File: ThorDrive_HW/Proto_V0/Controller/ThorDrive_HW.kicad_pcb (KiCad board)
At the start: 2 copper layers, 98.5 x 99 mm, 46 parts, among them J1 Conn_01x04_Socket, J10 Conn_01x03_Socket, J2 Conn_01x06_Socket, J3 Conn_01x03_Socket, J4 Conn_01x08_Socket, J5 Conn_01x08_Pin, J6 Conn_01x04_Pin, J7 Conn_01x06_Pin, J8 Conn_01x04_Pin, J9 Conn_01x04_Pin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

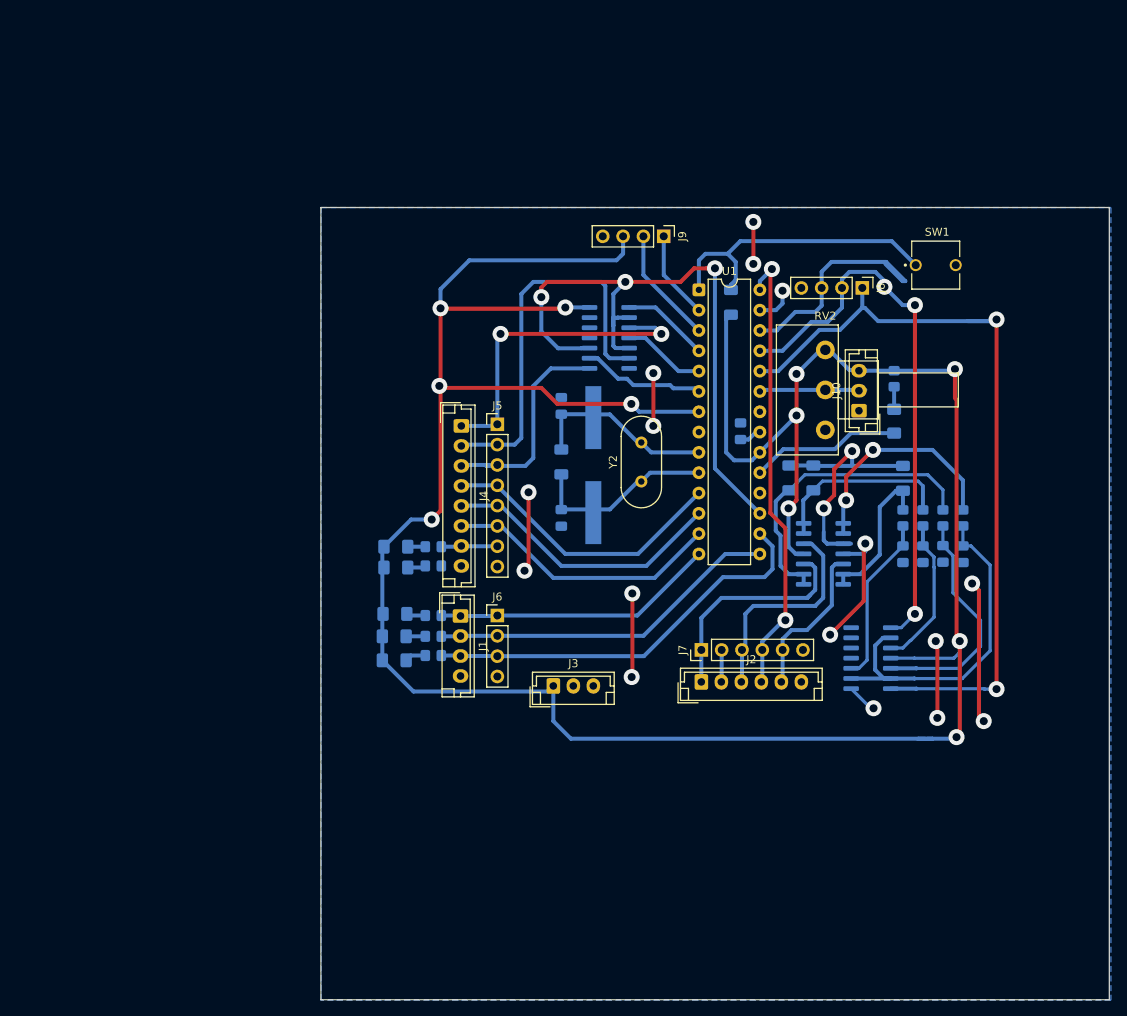
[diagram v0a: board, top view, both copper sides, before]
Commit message: Controller Board V0 Finalized
A Controller Board simple and built upon the Atmega328p...
Single Layer Design with few jumpers.... Compatible with Inverter V0
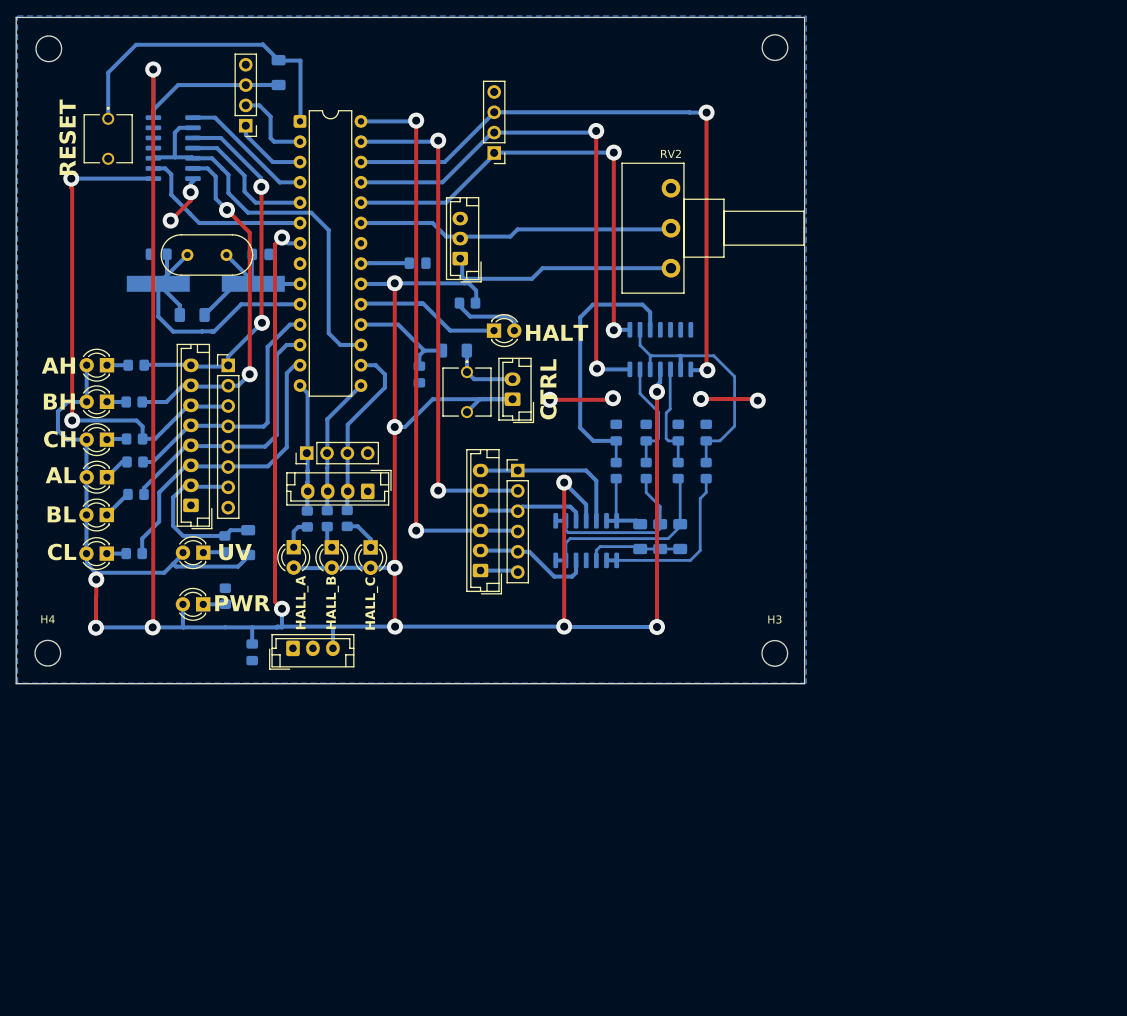
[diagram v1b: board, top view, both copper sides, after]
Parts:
- added C8: 10u, Capacitor_SMD:C_0805_2012Metric_Pad1.18x1.45mm_HandSolder, B.Cu at (53.4, 100.8)
- added C9: 100n, Capacitor_SMD:C_0805_2012Metric_Pad1.18x1.45mm_HandSolder, B.Cu at (74.3, 66.1)
- added D10: AL, LED_THT:LED_D3.0mm, F.Cu at (35.2, 78.9)
- added D11: BL, LED_THT:LED_D3.0mm, F.Cu at (35.2, 83.6)
- added D12: CL, LED_THT:LED_D3.0mm, F.Cu at (35.2, 88.5)
- added D7: AH, LED_THT:LED_D3.0mm, F.Cu at (35.2, 64.9)
- added D8: BH, LED_THT:LED_D3.0mm, F.Cu at (35.2, 69.5)
- added D9: CH, LED_THT:LED_D3.0mm, F.Cu at (35.2, 74.2)
- added H1: MountingHole, MountingHole:MountingHole_3.2mm_M3, F.Cu at (27.9, 25.4)
- added H2: MountingHole, MountingHole:MountingHole_3.2mm_M3, F.Cu at (118.7, 25.2)
- added H3: MountingHole, MountingHole:MountingHole_3.2mm_M3, F.Cu at (118.7, 100.9)
- added H4: MountingHole, MountingHole:MountingHole_3.2mm_M3, F.Cu at (27.8, 100.9)
- added J13: CTRL, Connector_JST:JST_EH_B2B-EH-A_1x02_P2.50mm_Vertical, F.Cu at (85.9, 69.2)
- added R16: 1k, Resistor_SMD:R_0805_2012Metric_Pad1.20x1.40mm_HandSolder, B.Cu at (38.9, 64.9)
- added R17: 1k, Resistor_SMD:R_0805_2012Metric_Pad1.20x1.40mm_HandSolder, B.Cu at (38.6, 69.5)
- added R18: 1k, Resistor_SMD:R_0805_2012Metric_Pad1.20x1.40mm_HandSolder, B.Cu at (38.7, 74.1)
- added R19: 1k, Resistor_SMD:R_0805_2012Metric_Pad1.20x1.40mm_HandSolder, B.Cu at (38.7, 77.0)
- added R20: 1k, Resistor_SMD:R_0805_2012Metric_Pad1.20x1.40mm_HandSolder, B.Cu at (38.8, 81.1)
- added R21: 1k, Resistor_SMD:R_0805_2012Metric_Pad1.20x1.40mm_HandSolder, B.Cu at (38.6, 88.5)
- added R22: 10k, Resistor_SMD:R_1206_3216Metric_Pad1.30x1.75mm_HandSolder, B.Cu at (52.9, 87.1)
- added R23: 10k, Resistor_SMD:R_1206_3216Metric_Pad1.30x1.75mm_HandSolder, B.Cu at (78.6, 63.1)
- added SW3: CTRL, libMain:SW_BUTT-2, F.Cu at (80.2, 68.3)
- D1: value Fault -> HALT; footprint LED_SMD:LED_1206_3216Metric_Pad1.42x1.75mm_HandSolder -> LED_THT:LED_D3.0mm; moved to F.Cu
- D2: value LED -> HALL_A; footprint LED_SMD:LED_1206_3216Metric_Pad1.42x1.75mm_HandSolder -> LED_THT:LED_D3.0mm; moved to F.Cu
- D3: value LED -> HALL_C; footprint LED_SMD:LED_1206_3216Metric_Pad1.42x1.75mm_HandSolder -> LED_THT:LED_D3.0mm; moved to F.Cu
- D4: value LED -> HALL_B; footprint LED_SMD:LED_1206_3216Metric_Pad1.42x1.75mm_HandSolder -> LED_THT:LED_D3.0mm; moved to F.Cu
- D5: value LED -> PWR; footprint LED_SMD:LED_1206_3216Metric_Pad1.42x1.75mm_HandSolder -> LED_THT:LED_D3.0mm; moved to F.Cu
- D6: value LED -> UV; footprint LED_SMD:LED_1206_3216Metric_Pad1.42x1.75mm_HandSolder -> LED_THT:LED_D3.0mm; moved to F.Cu
- SW1: value SW_Push -> RESET
- moved SW1 104.6 mm to (35.4, 36.6), turned to -90 degrees
- moved R2 63.4 mm to (56.7, 28.3)
- moved Y2 63.4 mm to (45.3, 51.1), turned to 0 degrees
- moved C2 60.2 mm to (41.7, 51.0), turned to 180 degrees
- moved U4 59.5 mm to (43.5, 37.8)
- moved R10 54.2 mm to (80.3, 57.1), turned to 180 degrees
- moved U1 54.1 mm to (59.3, 34.4)
- moved J9 54.0 mm to (52.6, 35.0), turned to 180 degrees
- moved Y1 53.5 mm to (47.6, 54.7), turned to 0 degrees
- moved J10 53.3 mm to (79.4, 51.6)
- moved D1 51.3 mm to (83.6, 60.6), turned to 0 degrees
- moved R1 49.7 mm to (45.9, 58.6), turned to 180 degrees
- moved J8 49.0 mm to (83.6, 38.4), turned to 180 degrees
- moved U2 46.7 mm to (104.4, 63.0), turned to 90 degrees
- moved C7 45.5 mm to (74.0, 52.2), turned to 0 degrees
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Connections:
- C4 pad 1: Net-(U2B-+) -> Net-(U2C-+)
- C5 pad 1: Net-(U2A-+) -> Net-(U2B--)
- C6 pad 1: Net-(U2C-+) -> Net-(U2A-+)
- J1 pad 1: HallA -> GND
- J1 pad 2: HallB -> HallC
- J1 pad 3: HallC -> HallB
- J1 pad 4: GND -> HallA
- J10 pad 1: GND -> +5V
- J10 pad 3: +5V -> GND
- J2 pad 1: PhaseA voltage -> GND
- J2 pad 2: PhaseA current -> PhaseC voltage
- J2 pad 3: PhaseB voltage -> PhaseB current
- J2 pad 4: PhaseB current -> PhaseB voltage
- J2 pad 5: PhaseC voltage -> PhaseA current
- J2 pad 6: GND -> PhaseA voltage
- J3 pad 1: +5V -> GND
- J3 pad 3: GND -> +5V
- J4 pad 1: /Logic_AH -> GND
- J4 pad 2: /Logic_BH -> Fault
- J4 pad 3: /Logic_CH -> /Logic_CL
- J4 pad 4: /Logic_AL -> /Logic_BL
- J4 pad 5: /Logic_BL -> /Logic_AL
- J4 pad 6: /Logic_CL -> /Logic_CH
- J4 pad 7: Fault -> /Logic_BH
- J4 pad 8: GND -> /Logic_AH
- J9 pad 1: RX -> TX
- J9 pad 2: TX -> RX
- R7 pad 2: Net-(U2B-+) -> Net-(U2C-+)
- R8 pad 2: Net-(U2A-+) -> Net-(U2B--)
- R9 pad 2: Net-(U2C-+) -> Net-(U2A-+)
- RV2 pad 1: GND -> +5V
- RV2 pad 3: +5V -> GND
- U1 pad 18: unconnected-(U1-PB4-Pad18) -> CTRL_BUTT
- U2 pad 1: emfZCD_B -> emfZCS_C
- U2 pad 5: Net-(U2B-+) -> VN_voltageBuffFilt
- U2 pad 6: VN_voltageBuffFilt -> Net-(U2B--)
- U2 pad 7: emfZCD_A -> emfZCD_B
- U2 pad 8: emfZCS_C -> emfZCD_A
- U3 pad 1: AG_voltageBuff -> BG_voltageBuff
- U3 pad 2: AG_voltageBuff -> BG_voltageBuff
- U3 pad 3: PhaseA voltage -> PhaseB voltage
- U3 pad 5: PhaseB voltage -> PhaseA voltage
- U3 pad 6: BG_voltageBuff -> AG_voltageBuff
- U3 pad 7: BG_voltageBuff -> AG_voltageBuff
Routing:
- net +5V: track 344.0 -> 467.5 mm, vias 11 -> 14
- net PhaseA current: track 8.80 -> 63.4 mm, vias 1 -> 2
- net GND: track 76.9 -> 26.0 mm, vias 14 -> 6
- net emfZCS_C: track 32.5 -> 80.2 mm, vias 1 -> 2
- net emfZCD_A: track 99.5 -> 58.5 mm
- net /Logic_CH: track 27.6 -> 63.7 mm, vias 0 -> 2
- net speed: track 81.7 -> 50.2 mm, vias 3 -> 0
- net Net-(U2B-+): track 29.9 -> 0.00 mm
- net HallC: track 51.1 -> 22.4 mm
- net AG_voltageBuff: track 38.2 -> 9.71 mm
- net HallB: track 44.1 -> 17.3 mm
- net pot: track 13.3 -> 39.9 mm
- net VN: track 32.7 -> 12.0 mm, vias 2 -> 0
- net HallA: track 35.4 -> 16.1 mm
- net Net-(U1-XTAL2/PB7): track 23.5 -> 38.6 mm
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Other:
- board size 98.5 x 99 mm -> 98.5 x 83.3 mm
- board text added: "Conn_01x08_Pin"

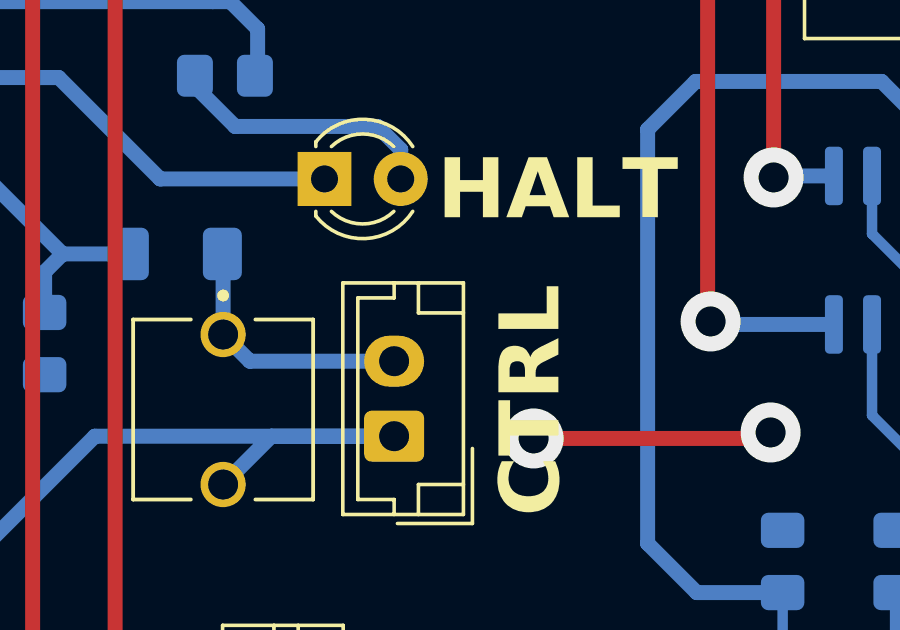
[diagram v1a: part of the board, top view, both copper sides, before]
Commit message: Latest hardware  changes (added pulldown Resistor for CTRL button)
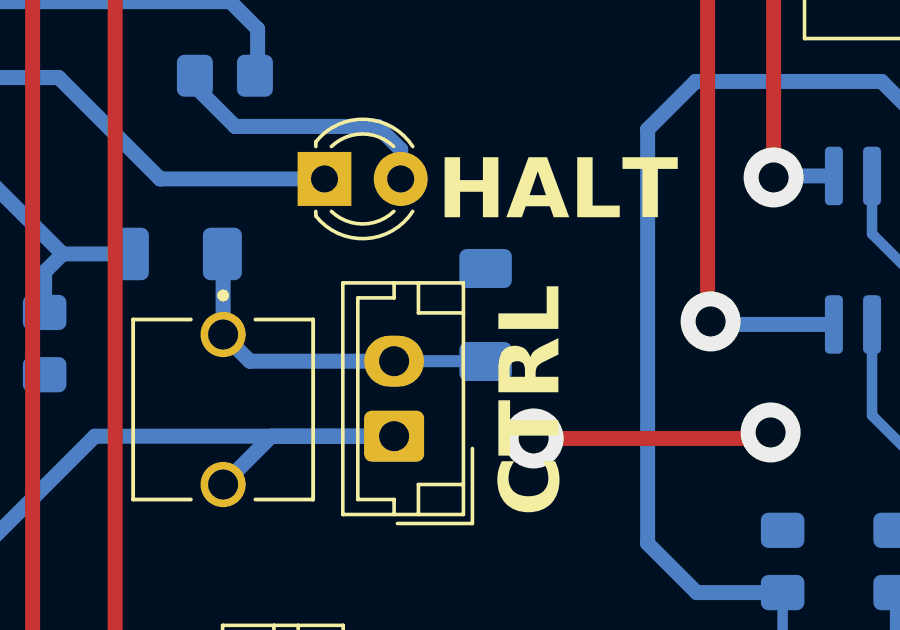
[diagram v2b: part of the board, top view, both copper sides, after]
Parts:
- added R24: 10k, Resistor_SMD:R_1206_3216Metric_Pad1.30x1.75mm_HandSolder, B.Cu at (89.0, 65.1)
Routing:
- net Net-(J13-Pin_2): track 8.76 -> 11.8 mm
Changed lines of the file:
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@@
 		(allow_soldermask_bridges_in_footprints no)
 		(tenting front back)
+		(aux_axis_origin 23.8575 104.72)
+		(grid_origin 23.8575 104.72)
 		(pcbplotparams
 			(layerselection 0x00000000_00000000_55555555_5755f5ff)
@@
 			(plotframeref no)
 			(mode 1)
-			(useauxorigin no)
+			(useauxorigin yes)
 			(hpglpennumber 1)
 			(hpglpenspeed 20)
@@
 			(outputformat 1)
 			(mirror no)
-			(drillshape 1)
+			(drillshape 0)
 			(scaleselection 1)
-			(outputdirectory "")
+			(outputdirectory "Fab/")
 		)
 	)
@@
 			)
 			(layer "F.SilkS")
-			(net 56)
 		)
 		(fp_line
@@
 			)
 			(layer "F.SilkS")
-			(net 56)
 		)
 		(fp_arc
@@
 			)
 			(layer "F.SilkS")
-			(net 56)
 		)
 		(fp_arc
@@
 			)
 			(layer "F.SilkS")
-			(net 56)
 		)
 		(fp_arc
@@
 			)
 			(layer "F.SilkS")
-			(net 56)
 		)
 		(fp_arc
@@
 			)
 			(layer "F.SilkS")
-			(net 56)
 		)
 		(fp_line
@@
 			)
 			(layer "F.CrtYd")
-			(net 56)
 		)
 		(fp_line
@@
 			)
 			(layer "F.CrtYd")
-			(net 56)
 		)
 		(fp_line
@@
 			)
 			(layer "F.CrtYd")
-			(net 56)
 		)
 		(fp_line
@@
 			)
 			(layer "F.CrtYd")
-			(net 56)
 		)
 		(fp_line
@@
 			)
 			(layer "F.Fab")
-			(net 56)
 		)
 		(fp_arc
@@
 			)
 			(layer "F.Fab")
-			(net 56)
 		)
 		(fp_circle
@@
 			(fill no)
 			(layer "F.Fab")
-			(net 56)
 		)
 		(fp_text user "${REFERENCE}"
@@
 		)
 	)
+	(footprint "Resistor_SMD:R_1206_3216Metric_Pad1.30x1.75mm_HandSolder"
+		(layer "B.Cu")
+		(at 88.9575 65.12 -90)
+		(descr "Resistor SMD 1206 (3216 Metric), square (rectangular) end terminal, IPC_7351 nominal with elongated pad for handsoldering. (Body size source: IPC-SM-782 page 72, https://www.pcb-3d.com/wordpress/wp-content/uploads/ipc-sm-782a_amendment_1_and_2.pdf), generated with kicad-footprint-generator")
+		(tags "resistor handsolder")
+		(property "Reference" "R24"
+			(at 0 1.82 90)
+			(layer "B.SilkS")
+			(effects
+				(font
+					(size 1 1)
+					(thickness 0.15)
+				)
+				(justify mirror)
+			)
+		)
+		(property "Value" "10k"
+			(at 0 -1.82 90)
+			(layer "B.Fab")
+			(effects
+				(font
+					(size 1 1)
+					(thickness 0.15)
+				)
+				(justify mirror)
+			)
+		)
+		(property "Datasheet" ""
+			(at 0 0 90)
+			(unlocked yes)
+			(layer "B.Fab")
+			(hide yes)
+			(effects
+				(font
+					(size 1.27 1.27)
+					(thickness 0.15)
+				)
+				(justify mirror)
+			)
+		)
+		(property "Description" "Resistor"
+			(at 0 0 90)
+			(unlocked yes)
+			(layer "B.Fab")
+			(hide yes)
+			(effects
+				(font
+					(size 1.27 1.27)
+					(thickness 0.15)
+				)
+				(justify mirror)
+			)
+		)
+		(property ki_fp_filters "R_*")
+		(sheetname "/")
+		(sheetfile "ThorDrive_HW.kicad_sch")
+		(attr smd)
+		(fp_line
+			(start -0.727064 0.91)
+			(end 0.727064 0.91)
+			(stroke
+				(width 0.12)
+				(type solid)
+			)
+			(layer "B.SilkS")
+		)
+		(fp_line
+			(start -0.727064 -0.91)
+			(end 0.727064 -0.91)
+			(stroke
+				(width 0.12)
+				(type solid)
+			)
+			(layer "B.SilkS")
+		)
+		(fp_line
+			(start -2.45 1.12)
+			(end 2.45 1.12)
+			(stroke
+				(width 0.05)
+				(type solid)
+			)
+			(layer "B.CrtYd")
+		)
+		(fp_line
+			(start 2.45 1.12)
+			(end 2.45 -1.12)
+			(stroke
+				(width 0.05)
+				(type solid)
+			)
+			(layer "B.CrtYd")
+		)
+		(fp_line
+			(start -2.45 -1.12)
+			(end -2.45 1.12)
+			(stroke
+				(width 0.05)
+				(type solid)
+			)
+			(layer "B.CrtYd")
+		)
+		(fp_line
+			(start 2.45 -1.12)
+			(end -2.45 -1.12)
+			(stroke
+				(width 0.05)
+				(type solid)
+			)
+			(layer "B.CrtYd")
+		)
+		(fp_line
+			(start -1.6 0.8)
+			(end 1.6 0.8)
+			(stroke
+				(width 0.1)
+				(type solid)
+			)
+			(layer "B.Fab")
+		)
+		(fp_line
+			(start 1.6 0.8)
+			(end 1.6 -0.8)
+			(stroke
+				(width 0.1)
+				(type solid)
+			)
+			(layer "B.Fab")
+		)
+		(fp_line
+			(start -1.6 -0.8)
+			(end -1.6 0.8)
+			(stroke
+				(width 0.1)
+				(type solid)
+			)
+			(layer "B.Fab")
+		)
+		(fp_line
+			(start 1.6 -0.8)
+			(end -1.6 -0.8)
+			(stroke
+				(width 0.1)
+				(type solid)
+			)
+			(layer "B.Fab")
+		)
+		(fp_text user "${REFERENCE}"
+			(at 0 0 90)
+			(layer "B.Fab")
+			(effects
+				(font
+					(size 0.8 0.8)
+					(thickness 0.12)
+				)
+				(justify mirror)
+			)
+		)
+		(pad "1" smd roundrect
+			(at -1.55 0 270)
+			(size 1.3 1.75)
+			(layers "B.Cu" "B.Mask" "B.Paste")
+			(roundrect_rratio 0.192308)
+			(net 1 "GND")
+			(pintype "passive")
+		)
+		(pad "2" smd roundrect
+			(at 1.55 0 270)
+			(size 1.3 1.75)
+			(layers "B.Cu" "B.Mask" "B.Paste")
+			(roundrect_rratio 0.192308)
+			(net 62 "Net-(J13-Pin_2)")
+			(pintype "passive")
+		)
+		(embedded_fonts no)
+		(model "${KICAD9_3DMODEL_DIR}/Resistor_SMD.3dshapes/R_1206_3216Metric.wrl"
+			(offset
+				(xyz 0 0 0)
+			)
+			(scale
+				(xyz 1 1 1)
+			)
+			(rotate
+				(xyz 0 0 0)
+			)
+		)
+	)
 	(footprint "Package_SO:SOIC-14_3.9x8.7mm_P1.27mm"
 		(layer "B.Cu")
@@
 			)
 			(layer "B.SilkS")
-			(net 56)
 		)
 		(fp_line
@@
 			)
 			(layer "B.SilkS")
-			(net 56)
 		)
 		(fp_line
@@
 			)
 			(layer "B.CrtYd")
-			(net 56)
 		)
 		(fp_line
@@
 			)
 			(layer "B.CrtYd")
-			(net 56)
 		)
 		(fp_line
@@
 			)
 			(layer "B.CrtYd")
-			(net 56)
 		)
 		(fp_line
@@
 			)
 			(layer "B.CrtYd")
-			(net 56)
 		)
 		(fp_line
@@
 			)
 			(layer "B.Fab")
-			(net 56)
 		)
 		(fp_line
@@
 			)
 			(layer "B.Fab")
-			(net 56)
 		)
 		(fp_line
@@
 			)
 			(layer "B.Fab")
-			(net 56)
 		)
 		(fp_line
@@
 			)
 			(layer "B.Fab")
-			(net 56)
 		)
 		(fp_text user "${REFERENCE}"
@@
 	)
 	(segment
+		(start 88.9475 66.66)
+		(end 88.9575 66.67)
+		(width 0.4)
+		(layer "B.Cu")
+		(net 62)
+	)
+	(segment
 		(start 80.2075 63.11)
 		(end 80.1825 63.085)
@@
 		(layer "B.Cu")
 		(net 62)
+	)
+	(segment
+		(start 85.9075 66.66)
+		(end 88.9475 66.66)
+		(width 0.4)
+		(layer "B.Cu")
+		(net 62)
